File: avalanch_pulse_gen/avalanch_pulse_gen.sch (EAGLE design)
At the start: 0 parts

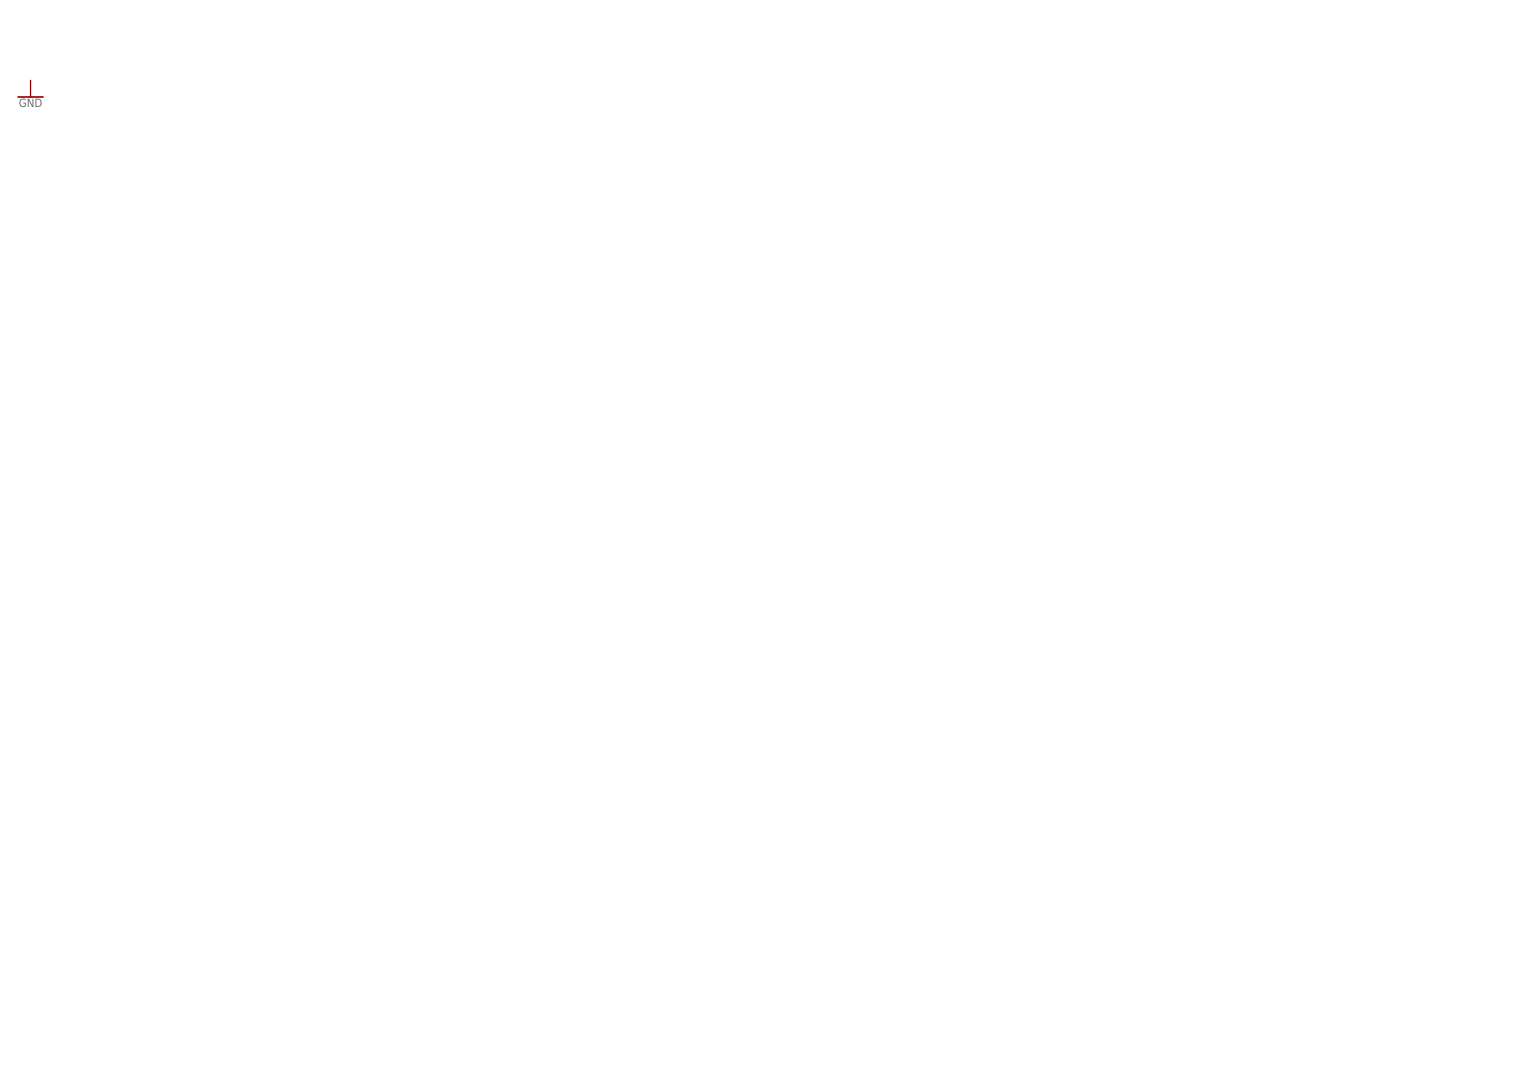
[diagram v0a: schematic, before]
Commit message: diddled the simulation bits until everything looked good, made some tweaks to the schematic, and did the board layout. Generated Gerbers to hand off to 3PCB.
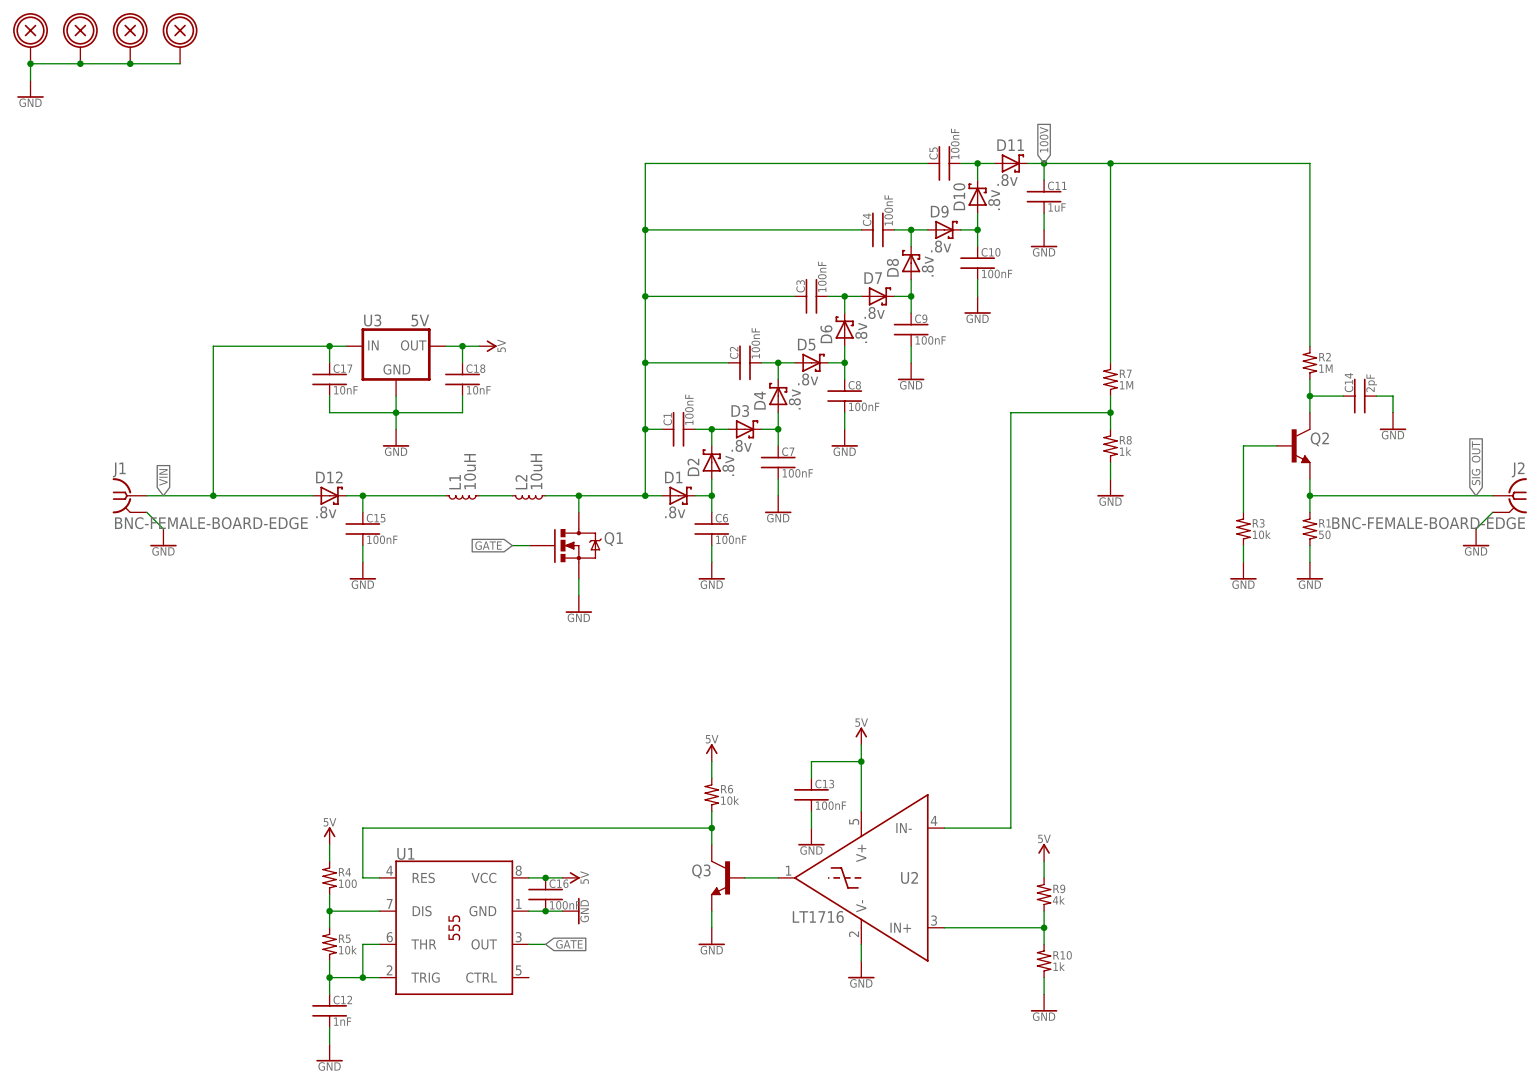
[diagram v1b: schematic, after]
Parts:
- added C1, C10, C15, C2, C3, C4, C5, C6, C7, C8, C9: 100nF, jack_RCL:CAP_SMD_1206
- added C11: 1uF, jack_RCL:CAP_SMD_2220
- added C12: 1nF, jack_RCL:CAP_SMD_0402
- added C13, C16: 100nF, jack_RCL:CAP_SMD_0402
- added C14: 2pF, jack_RCL:CAP_SMD_0805
- added C17, C18: 10nF, jack_RCL:CAP_SMD_0402
- added D1, D10, D11, D12, D2, D3, D4, D5, D6, D7, D8, D9: .8v, jack_semi:SCHOTTKY_SOD-123
- added H1, H2, H3, H4: BOLTHOLE_M2.5, jack_mechanical:BOLTHOLE_M2.5
- added J1, J2: BNC-FEMALE-BOARD-EDGE, jack_connector:BNC-FEMALE-BOARD-EDGE
- added L1, L2: 10uH, jack_RCL:IND_SMD_WE74405031100
- added Q1: (no value), jack_semi:MOSFET_N-CHANNEL_SOT23-3
- added Q2, Q3: (no value), jack_semi:BJT_NPN
- added R1: 50, jack_RCL:RES_SMD_0402
- added R10, R8: 1k, jack_RCL:RES_SMD_0402
- added R2, R7: 1M, jack_RCL:RES_SMD_1206
- added R3, R5, R6: 10k, jack_RCL:RES_SMD_0402
- added R4: 100, jack_RCL:RES_SMD_0402
- added R9: 4k, jack_RCL:RES_SMD_0402
- added U1: 555_TIMER_SOIC-8, jack_IC:555_TIMER_SOIC-8
- added U2: LT1716, jack_IC:LT1716
- added U3: 5V, jack_IC:UAMXX-Q1DCY
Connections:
- new net 100V: C11.1, D11.C, R2.1, R7.1
- new net 5V: C13.1, C16.1, C18.1, R4.1, R6.1, R9.1, U1.VCC, U2.V+, U3.OUT
- new net GATE: Q1.G, U1.OUT
- new net GND: C10.2, C11.2, C12.2, C13.2, C14.2, C15.2, C16.2, C17.2, C18.2, C6.2, C7.2, C8.2, C9.2, H1.P, H2.P, H3.P, H4.P, J1.GND, J2.GND, Q1.S, Q3.E, R1.2, R10.2, R3.2, R8.2, U1.GND, U2.V-, U3.GND
- new net N$1: C6.1, D1.C, D2.A
- new net N$10: C10.1, D10.A, D9.C
- new net N$11: C5.2, D10.C, D11.A
- new net N$12: C12.1, R5.2, U1.THR, U1.TRIG
- new net N$13: Q2.B, R3.1
- new net N$14: C14.1, Q2.C, R2.2
- new net N$15: R4.2, R5.1, U1.DIS
- new net N$16: Q3.C, R6.2, U1.RES
- new net N$17: Q3.B, U2.OUT
- new net N$18: R7.2, R8.1, U2.IN-
- new net N$19: R10.1, R9.2, U2.IN+
- new net N$2: C1.2, D2.C, D3.A
- new net N$20: C15.1, D12.C, L1.1
- new net N$21: L1.2, L2.1
- new net N$3: C2.2, D4.C, D5.A
- new net N$4: C7.1, D3.C, D4.A
- new net N$5: C8.1, D5.C, D6.A
- new net N$6: C1.1, C2.1, C3.1, C4.1, C5.1, D1.A, L2.2, Q1.D
- new net N$7: C3.2, D6.C, D7.A
- new net N$8: C9.1, D7.C, D8.A
- new net N$9: C4.2, D8.C, D9.A
- new net SIG_OUT: J2.1, Q2.E, R1.1
- new net VIN: C17.1, D12.A, J1.1, U3.IN
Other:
- note added: "50_OHM_SE"
